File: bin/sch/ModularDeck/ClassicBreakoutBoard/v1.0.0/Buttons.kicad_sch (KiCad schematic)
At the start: 2 parts

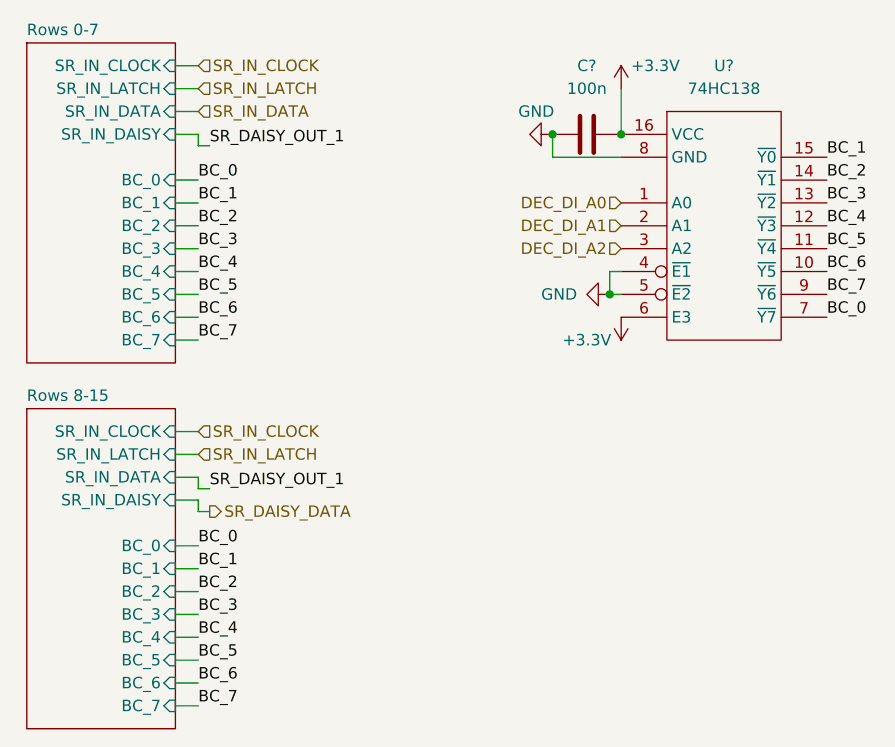
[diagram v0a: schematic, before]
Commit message: Finalised schematics for ModularDeck v1.0.0 (but probably really 0.0.1
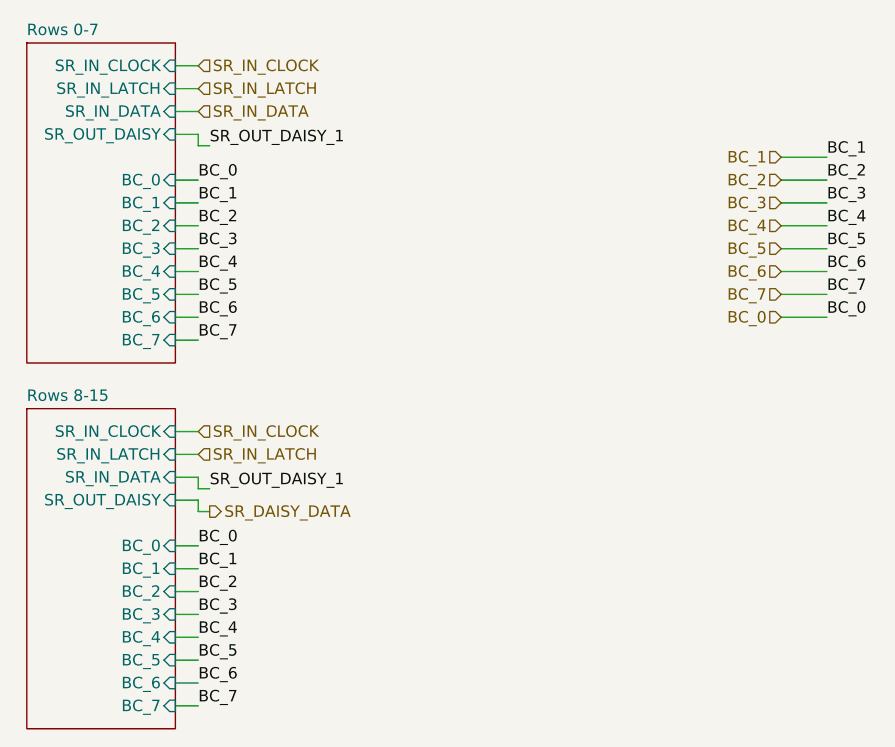
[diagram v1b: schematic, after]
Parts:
- removed C?: 100n, Capacitor_SMD:C_0402_1005Metric, symbol Device:C
- removed U?: 74HC138, Package_SO:SO-16_3.9x9.9mm_P1.27mm, symbol igor_lib:74HC138
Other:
- sheet Rows 0-7 ports: added SR_OUT_DAISY; removed SR_IN_DAISY
- sheet Rows 8-15 ports: added SR_OUT_DAISY; removed SR_IN_DAISY
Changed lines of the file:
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@@
 (kicad_sch (version 20211123) (generator eeschema)
   (paper "A3")
-  (junction (at 105.41 58.42) (diameter 0) (color 0 0 0 0)
-  )
-  (junction (at 104.14 76.2) (diameter 0) (color 0 0 0 0)
-  )
-  (junction (at 97.79 58.42) (diameter 0) (color 0 0 0 0)
-  )
   (wire (pts (xy 55.88 81.28) (xy 58.42 81.28))
     (stroke (width 0) (type default) (color 0 0 0 0))
@@
     (stroke (width 0) (type default) (color 0 0 0 0))
   )
-  (wire (pts (xy 105.41 53.34) (xy 105.41 58.42))
-    (stroke (width 0) (type default) (color 0 0 0 0))
-  )
   (wire (pts (xy 55.88 99.06) (xy 58.42 99.06))
     (stroke (width 0) (type default) (color 0 0 0 0))
@@
     (stroke (width 0) (type default) (color 0 0 0 0))
   )
-  (wire (pts (xy 104.14 73.66) (xy 104.14 76.2))
+  (wire (pts (xy 123.19 78.74) (xy 128.27 78.74))
+    (stroke (width 0) (type default) (color 0 0 0 0))
+  )
+  (wire (pts (xy 123.19 76.2) (xy 128.27 76.2))
     (stroke (width 0) (type default) (color 0 0 0 0))
   )
@@
     (stroke (width 0) (type default) (color 0 0 0 0))
   )
-  (wire (pts (xy 105.41 73.66) (xy 104.14 73.66))
-    (stroke (width 0) (type default) (color 0 0 0 0))
-  )
   (wire (pts (xy 55.88 121.92) (xy 58.42 121.92))
     (stroke (width 0) (type default) (color 0 0 0 0))
@@
     (stroke (width 0) (type default) (color 0 0 0 0))
   )
+  (wire (pts (xy 123.19 68.58) (xy 128.27 68.58))
+    (stroke (width 0) (type default) (color 0 0 0 0))
+  )
   (wire (pts (xy 58.42 100.33) (xy 59.69 100.33))
     (stroke (width 0) (type default) (color 0 0 0 0))
@@
     (stroke (width 0) (type default) (color 0 0 0 0))
   )
+  (wire (pts (xy 123.19 71.12) (xy 128.27 71.12))
+    (stroke (width 0) (type default) (color 0 0 0 0))
+  )
   (wire (pts (xy 55.88 58.42) (xy 58.42 58.42))
     (stroke (width 0) (type default) (color 0 0 0 0))
@@
     (stroke (width 0) (type default) (color 0 0 0 0))
   )
+  (wire (pts (xy 123.19 73.66) (xy 128.27 73.66))
+    (stroke (width 0) (type default) (color 0 0 0 0))
+  )
   (wire (pts (xy 55.88 50.8) (xy 58.42 50.8))
     (stroke (width 0) (type default) (color 0 0 0 0))
   )
-  (wire (pts (xy 104.14 76.2) (xy 105.41 76.2))
+  (wire (pts (xy 123.19 60.96) (xy 128.27 60.96))
     (stroke (width 0) (type default) (color 0 0 0 0))
   )
@@
     (stroke (width 0) (type default) (color 0 0 0 0))
   )
-  (wire (pts (xy 105.41 60.96) (xy 97.79 60.96))
-    (stroke (width 0) (type default) (color 0 0 0 0))
-  )
   (wire (pts (xy 55.88 96.52) (xy 58.42 96.52))
     (stroke (width 0) (type default) (color 0 0 0 0))
@@
     (stroke (width 0) (type default) (color 0 0 0 0))
   )
+  (wire (pts (xy 123.19 66.04) (xy 128.27 66.04))
+    (stroke (width 0) (type default) (color 0 0 0 0))
+  )
+  (wire (pts (xy 123.19 63.5) (xy 128.27 63.5))
+    (stroke (width 0) (type default) (color 0 0 0 0))
+  )
   (wire (pts (xy 55.88 106.68) (xy 58.42 106.68))
     (stroke (width 0) (type default) (color 0 0 0 0))
@@
     (stroke (width 0) (type default) (color 0 0 0 0))
   )
-  (wire (pts (xy 97.79 60.96) (xy 97.79 58.42))
-    (stroke (width 0) (type default) (color 0 0 0 0))
-  )
   (wire (pts (xy 55.88 71.12) (xy 58.42 71.12))
     (stroke (width 0) (type default) (color 0 0 0 0))
@@
     (effects (font (size 1.27 1.27)) (justify left bottom))
   )
-  (label "SR_DAISY_OUT_1" (at 59.69 97.79 0)
+  (label "SR_OUT_DAISY_1" (at 59.69 97.79 0)
     (effects (font (size 1.27 1.27)) (justify left bottom))
   )
@@
     (effects (font (size 1.27 1.27)) (justify left bottom))
   )
-  (label "SR_DAISY_OUT_1" (at 59.69 59.69 0)
+  (label "SR_OUT_DAISY_1" (at 59.69 59.69 0)
     (effects (font (size 1.27 1.27)) (justify left bottom))
   )
@@
     (effects (font (size 1.27 1.27)) (justify left bottom))
   )
+  (hierarchical_label "BC_5" (shape input) (at 123.19 71.12 180)
+    (effects (font (size 1.27 1.27)) (justify right))
+  )
+  (hierarchical_label "BC_3" (shape input) (at 123.19 66.04 180)
+    (effects (font (size 1.27 1.27)) (justify right))
+  )
   (hierarchical_label "SR_IN_LATCH" (shape input) (at 58.42 93.98 0)
     (effects (font (size 1.27 1.27)) (justify left))
   )
+  (hierarchical_label "BC_2" (shape input) (at 123.19 63.5 180)
+    (effects (font (size 1.27 1.27)) (justify right))
+  )
   (hierarchical_label "SR_IN_CLOCK" (shape input) (at 58.42 50.8 0)
     (effects (font (size 1.27 1.27)) (justify left))
   )
+  (hierarchical_label "BC_6" (shape input) (at 123.19 73.66 180)
+    (effects (font (size 1.27 1.27)) (justify right))
+  )
+  (hierarchical_label "BC_4" (shape input) (at 123.19 68.58 180)
+    (effects (font (size 1.27 1.27)) (justify right))
+  )
+  (hierarchical_label "BC_7" (shape input) (at 123.19 76.2 180)
+    (effects (font (size 1.27 1.27)) (justify right))
+  )
   (hierarchical_label "SR_IN_CLOCK" (shape input) (at 58.42 91.44 0)
     (effects (font (size 1.27 1.27)) (justify left))
   )
-  (hierarchical_label "DEC_DI_A1" (shape input) (at 105.41 68.58 180)
-    (effects (font (size 1.27 1.27)) (justify right))
-  )
-  (hierarchical_label "DEC_DI_A0" (shape input) (at 105.41 66.04 180)
-    (effects (font (size 1.27 1.27)) (justify right))
-  )
-  (hierarchical_label "DEC_DI_A2" (shape input) (at 105.41 71.12 180)
+  (hierarchical_label "BC_1" (shape input) (at 123.19 60.96 180)
     (effects (font (size 1.27 1.27)) (justify right))
   )
@@
     (effects (font (size 1.27 1.27)) (justify left))
   )
-  (symbol (lib_id "power:+3.3V") (at 105.41 53.34 0) (unit 1)
-    (in_bom yes) (on_board yes)
-    (property "Reference" "#PWR?" (id 0) (at 105.41 57.15 0)
-      (effects (font (size 1.27 1.27)) hide)
-    )
-    (property "Value" "+3.3V" (id 1) (at 109.22 50.8 0))
-    (property "Footprint" "" (id 2) (at 105.41 53.34 0)
-      (effects (font (size 1.27 1.27)) hide)
-    )
-    (property "Datasheet" "" (id 3) (at 105.41 53.34 0)
-      (effects (font (size 1.27 1.27)) hide)
-    )
-    (pin "1")
-  )
-  (symbol (lib_id "Device:C") (at 101.6 58.42 90) (unit 1)
-    (in_bom yes) (on_board yes)
-    (property "Reference" "C?" (id 0) (at 101.6 50.8 90))
-    (property "Value" "100n" (id 1) (at 101.6 53.34 90))
-    (property "Footprint" "Capacitor_SMD:C_0402_1005Metric" (id 2) (at 105.41 57.4548 0)
-      (effects (font (size 1.27 1.27)) hide)
-    )
-    (property "Datasheet" "~" (id 3) (at 101.6 58.42 0)
-      (effects (font (size 1.27 1.27)) hide)
-    )
-    (property "LCSC" "C1525" (id 4) (at 101.6 58.42 0)
-      (effects (font (size 1.27 1.27)) hide)
-    )
-    (pin "1")
-    (pin "2")
-  )
-  (symbol (lib_id "power:GND") (at 97.79 58.42 270) (unit 1)
-    (in_bom yes) (on_board yes)
-    (property "Reference" "#PWR?" (id 0) (at 91.44 58.42 0)
-      (effects (font (size 1.27 1.27)) hide)
-    )
-    (property "Value" "GND" (id 1) (at 93.98 55.88 90)
-      (effects (font (size 1.27 1.27)) (justify left))
-    )
-    (property "Footprint" "" (id 2) (at 97.79 58.42 0)
-      (effects (font (size 1.27 1.27)) hide)
-    )
-    (property "Datasheet" "" (id 3) (at 97.79 58.42 0)
-      (effects (font (size 1.27 1.27)) hide)
-    )
-    (pin "1")
-  )
-  (symbol (lib_id "power:+3.3V") (at 105.41 78.74 180) (unit 1)
-    (in_bom yes) (on_board yes)
-    (property "Reference" "#PWR?" (id 0) (at 105.41 74.93 0)
-      (effects (font (size 1.27 1.27)) hide)
-    )
-    (property "Value" "+3.3V" (id 1) (at 101.6 81.28 0))
-    (property "Footprint" "" (id 2) (at 105.41 78.74 0)
-      (effects (font (size 1.27 1.27)) hide)
-    )
-    (property "Datasheet" "" (id 3) (at 105.41 78.74 0)
-      (effects (font (size 1.27 1.27)) hide)
-    )
-    (pin "1")
-  )
-  (symbol (lib_id "igor_lib:74HC138") (at 110.49 81.28 0) (unit 1)
-    (in_bom yes) (on_board yes) (fields_autoplaced)
-    (property "Reference" "U?" (id 0) (at 116.84 50.8 0))
-    (property "Value" "74HC138" (id 1) (at 116.84 53.34 0))
-    (property "Footprint" "Package_SO:SO-16_3.9x9.9mm_P1.27mm" (id 2) (at 116.84 66.04 0)
-      (effects (font (size 1.27 1.27)) hide)
-    )
-    (property "Datasheet" "" (id 3) (at 116.84 66.04 0)
-      (effects (font (size 1.27 1.27)) hide)
-    )
-    (property "LCSC" "C6818" (id 4) (at 110.49 81.28 0)
-      (effects (font (size 1.27 1.27)) hide)
-    )
-    (pin "16")
-    (pin "1")
-    (pin "10")
-    (pin "11")
-    (pin "12")
-    (pin "13")
-    (pin "14")
-    (pin "15")
-    (pin "2")
-    (pin "3")
-    (pin "4")
-    (pin "5")
-    (pin "6")
-    (pin "7")
-    (pin "8")
-    (pin "9")
-  )
-  (symbol (lib_id "power:GND") (at 104.14 76.2 270) (unit 1)
-    (in_bom yes) (on_board yes)
-    (property "Reference" "#PWR?" (id 0) (at 97.79 76.2 0)
-      (effects (font (size 1.27 1.27)) hide)
-    )
-    (property "Value" "GND" (id 1) (at 96.52 76.2 90)
-      (effects (font (size 1.27 1.27)) (justify left))
-    )
-    (property "Footprint" "" (id 2) (at 104.14 76.2 0)
-      (effects (font (size 1.27 1.27)) hide)
-    )
-    (property "Datasheet" "" (id 3) (at 104.14 76.2 0)
-      (effects (font (size 1.27 1.27)) hide)
-    )
-    (pin "1")
+  (hierarchical_label "BC_0" (shape input) (at 123.19 78.74 180)
+    (effects (font (size 1.27 1.27)) (justify right))
   )
   (sheet (at 39.37 48.26) (size 16.51 35.56) (fields_autoplaced)
@@
       (effects (font (size 1.27 1.27)) (justify right))
     )
-    (pin "SR_IN_DAISY" input (at 55.88 58.42 0)
+    (pin "SR_OUT_DAISY" input (at 55.88 58.42 0)
       (effects (font (size 1.27 1.27)) (justify right))
     )
@@
       (effects (font (size 1.27 1.27)) (justify right))
     )
-    (pin "SR_IN_DAISY" input (at 55.88 99.06 0)
-      (effects (font (size 1.27 1.27)) (justify right))
-    )
+    (pin "SR_OUT_DAISY" input (at 55.88 99.06 0)
+      (effects (font (size 1.27 1.27)) (justify right))
+    )
